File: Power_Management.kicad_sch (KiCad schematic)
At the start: 21 parts, among them J1 BATT, Q1 2N7002, SW1 POWER, U1 BQ24075RGT, U2 MAX17048

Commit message: feat(schematic): Add titles and individual sheet comments
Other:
- company: (none) -> Kurtis Lew
- title: (none) -> Conejo nRF52840 Keyboard - Power Management
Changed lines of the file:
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@@
 (kicad_sch (version 20211123) (generator eeschema)
   (paper "USLetter")
+  (title_block
+    (title "Conejo nRF52840 Keyboard - Power Management")
+    (company "Kurtis Lew")
+  )
   (junction (at 31.75 79.375) (diameter 0) (color 0 0 0 0)
   )

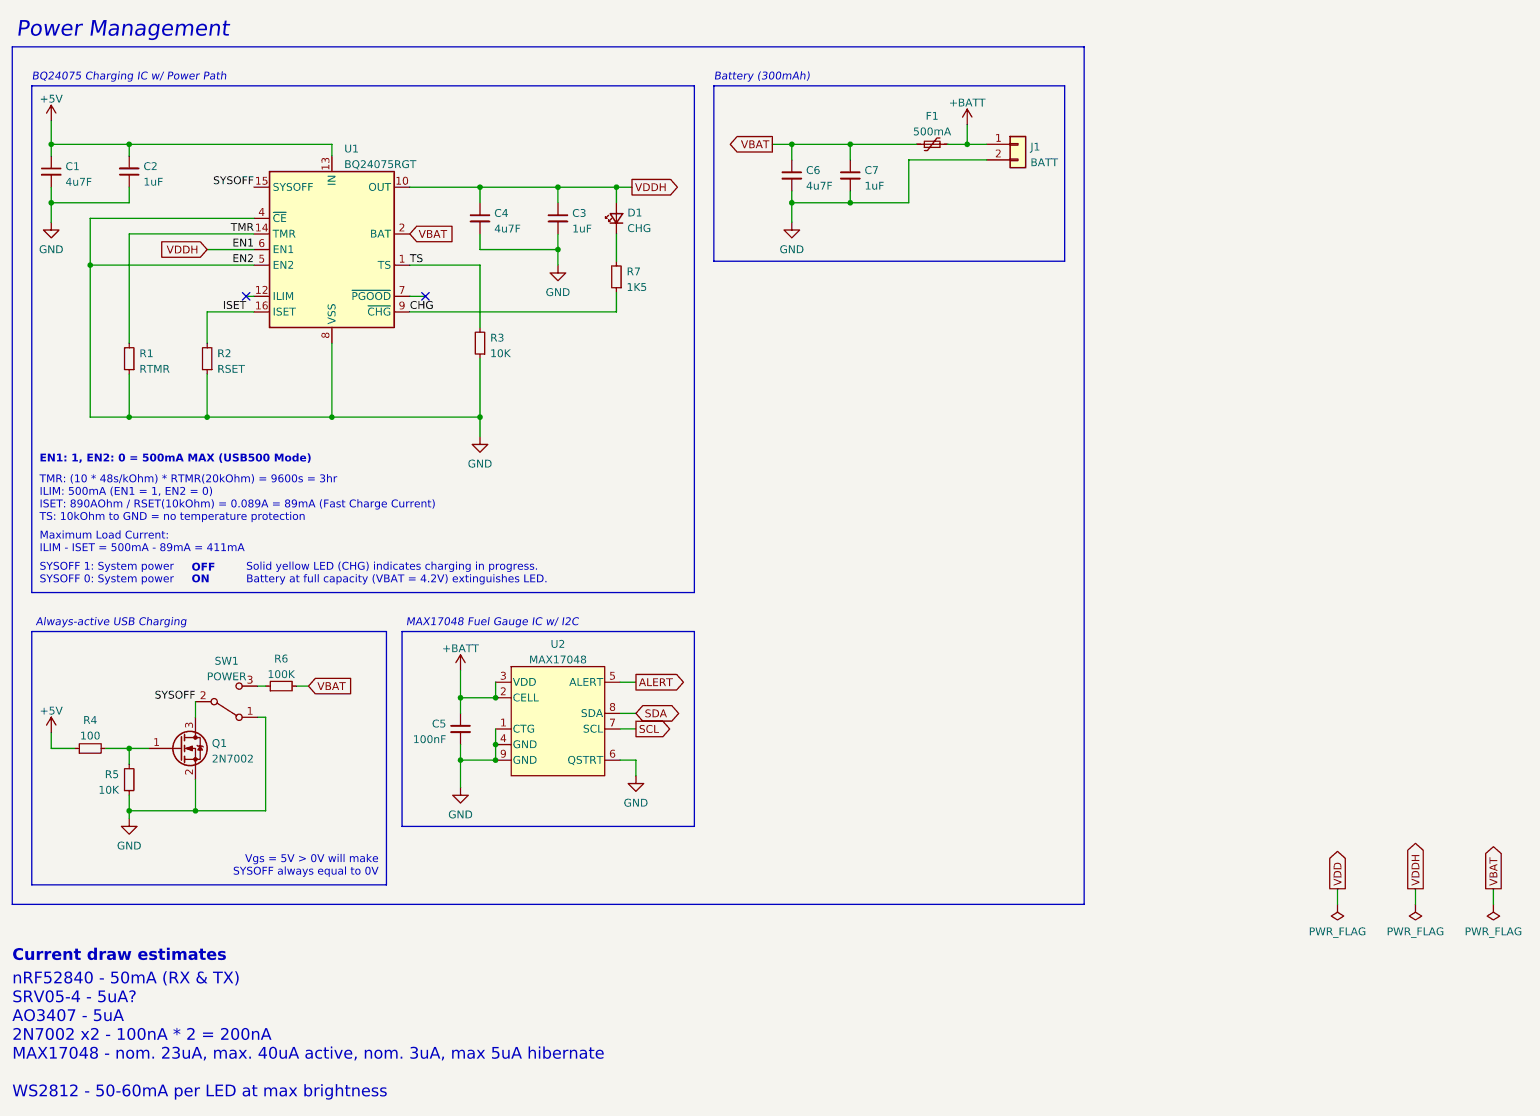
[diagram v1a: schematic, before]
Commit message: feat(pcb): Version 0.4
- Prepare to move from JLC7628 stackup to JLC3313 stackup (Lowers dielectric constant from 4.6 to 4.05)
- Increase mounting hole diameter back to 5.4mm
- 6mil signals, 10mil power, 13 mil vias
  - 3W spacing wherever possible
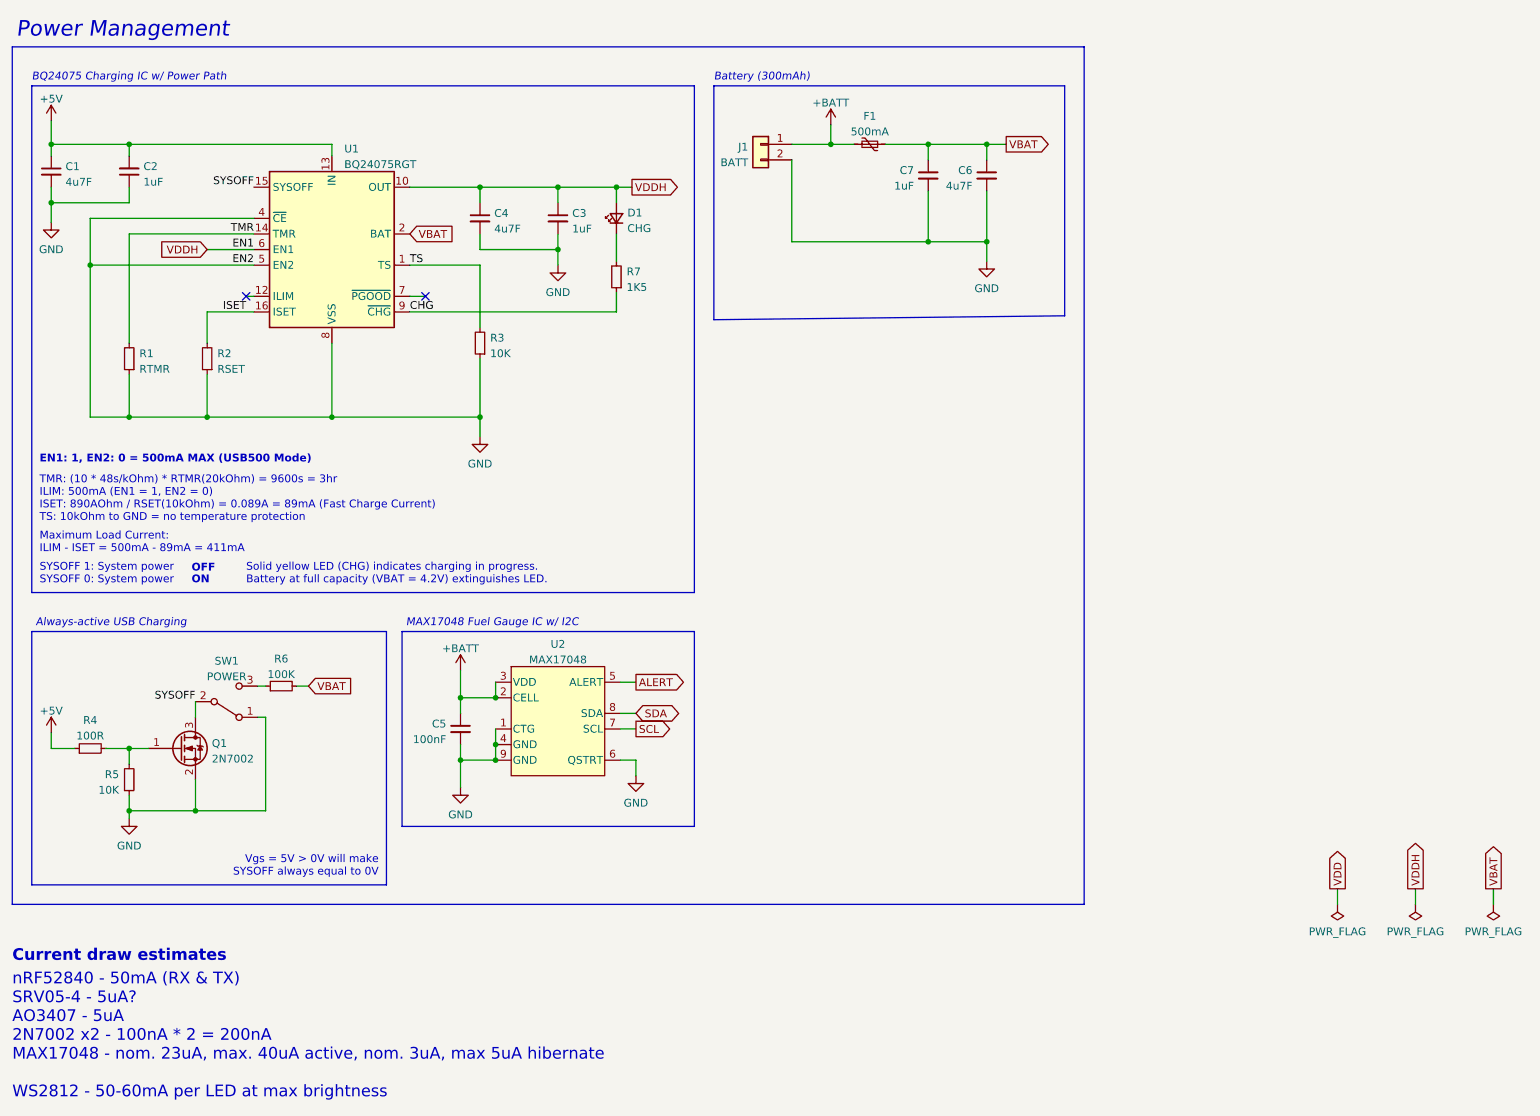
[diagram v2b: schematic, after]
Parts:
- R4: value 100 -> 100R
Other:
- moved on the sheet: C6, C7, F1, J1

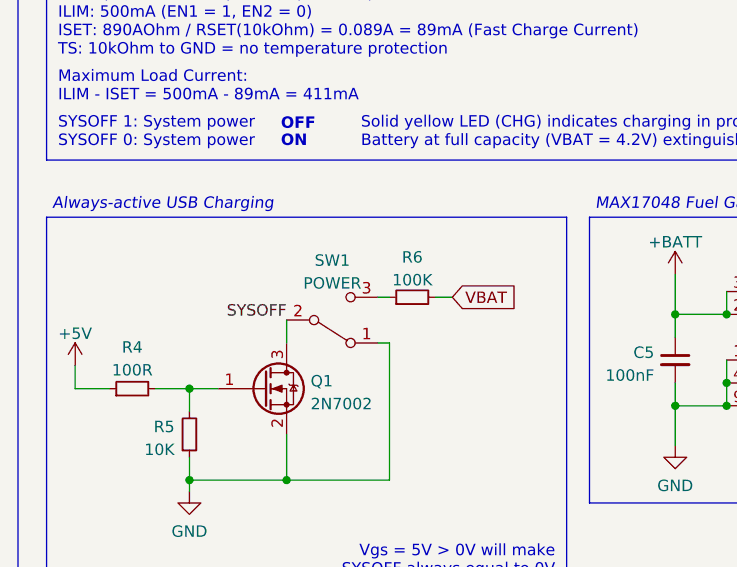
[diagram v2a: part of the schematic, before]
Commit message: feat(pcb): Version 0.4.1
- Add oscilloscope probing pads/labels
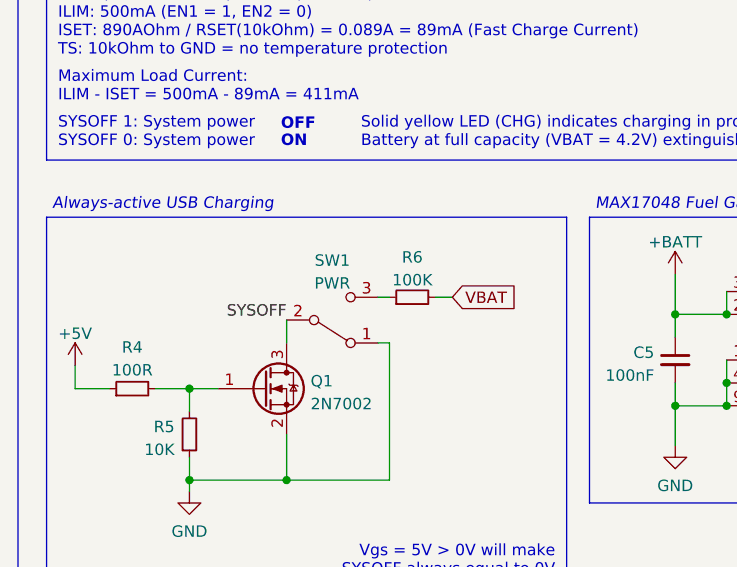
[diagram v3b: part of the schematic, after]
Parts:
- SW1: value POWER -> PWR
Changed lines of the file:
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@@
     (in_bom yes) (on_board yes) (fields_autoplaced)
     (property "Reference" "SW1" (id 0) (at 47.625 119.1092 0))
-    (property "Value" "POWER" (id 1) (at 47.625 121.6461 0))
+    (property "Value" "PWR" (id 1) (at 47.625 121.6461 0))
     (property "Footprint" "Conejo:SW_MSK12C02-HB (Reversible)" (id 2) (at 47.625 125.73 0)
       (effects (font (size 1.27 1.27)) hide)

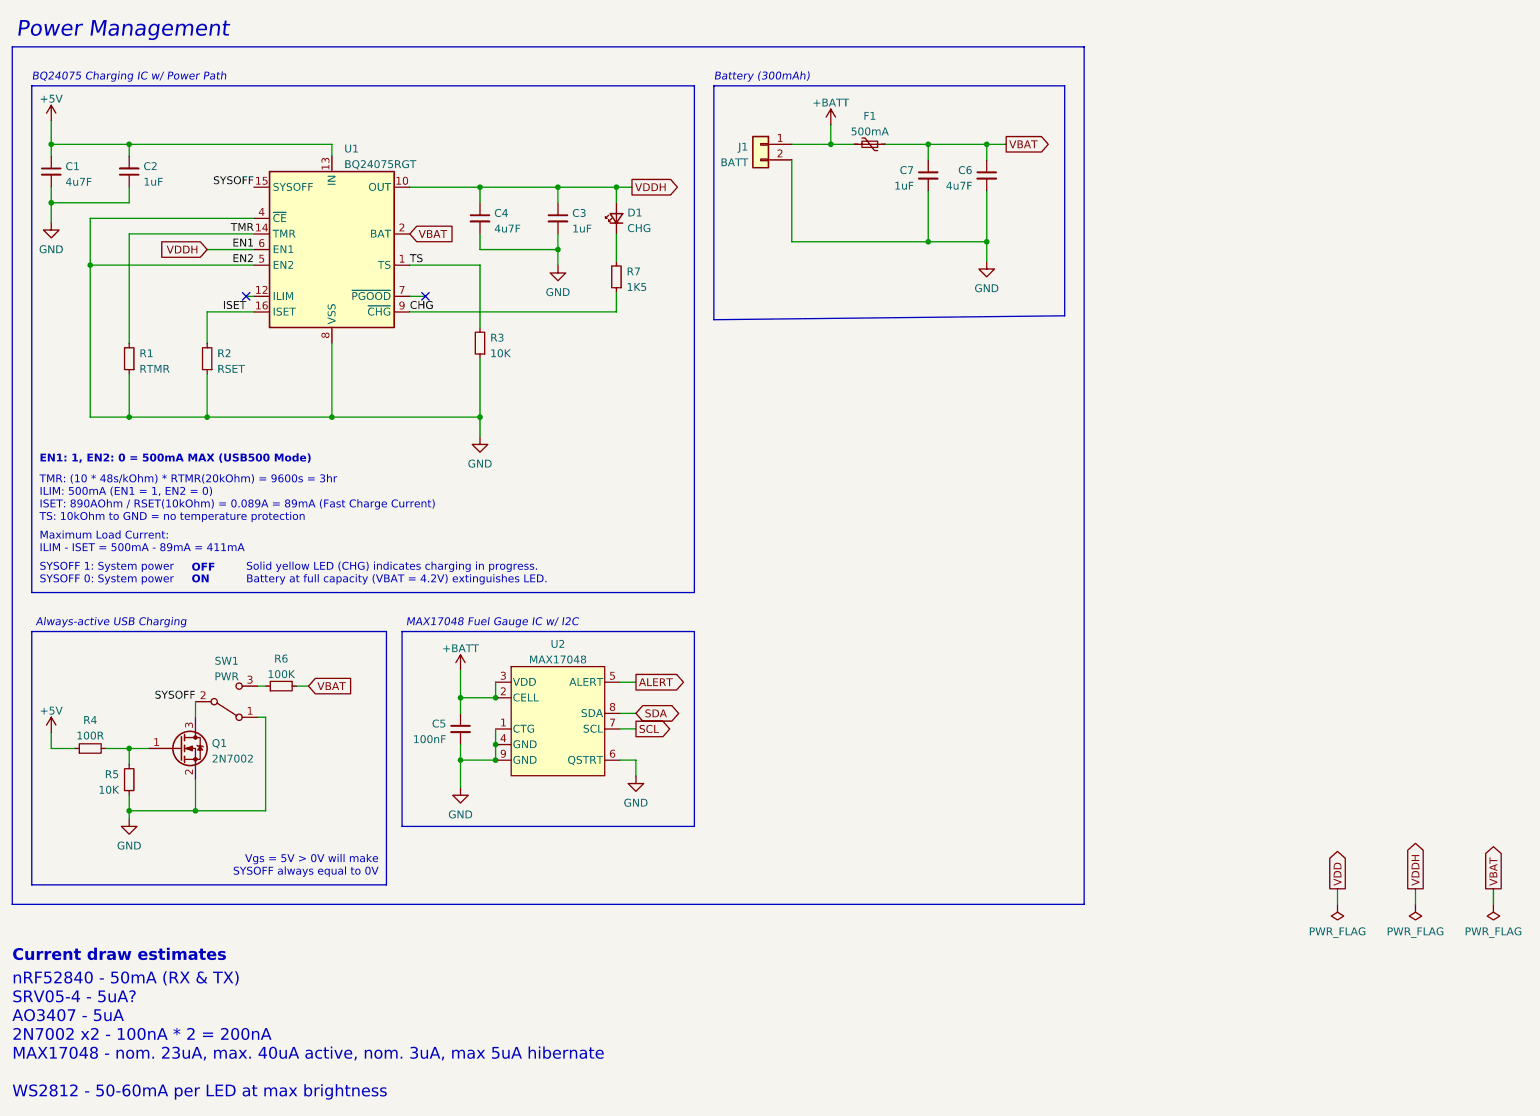
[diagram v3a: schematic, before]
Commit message: feat(pcb): Switch from 4.3mm NPTH mounting holes to M2 PTH
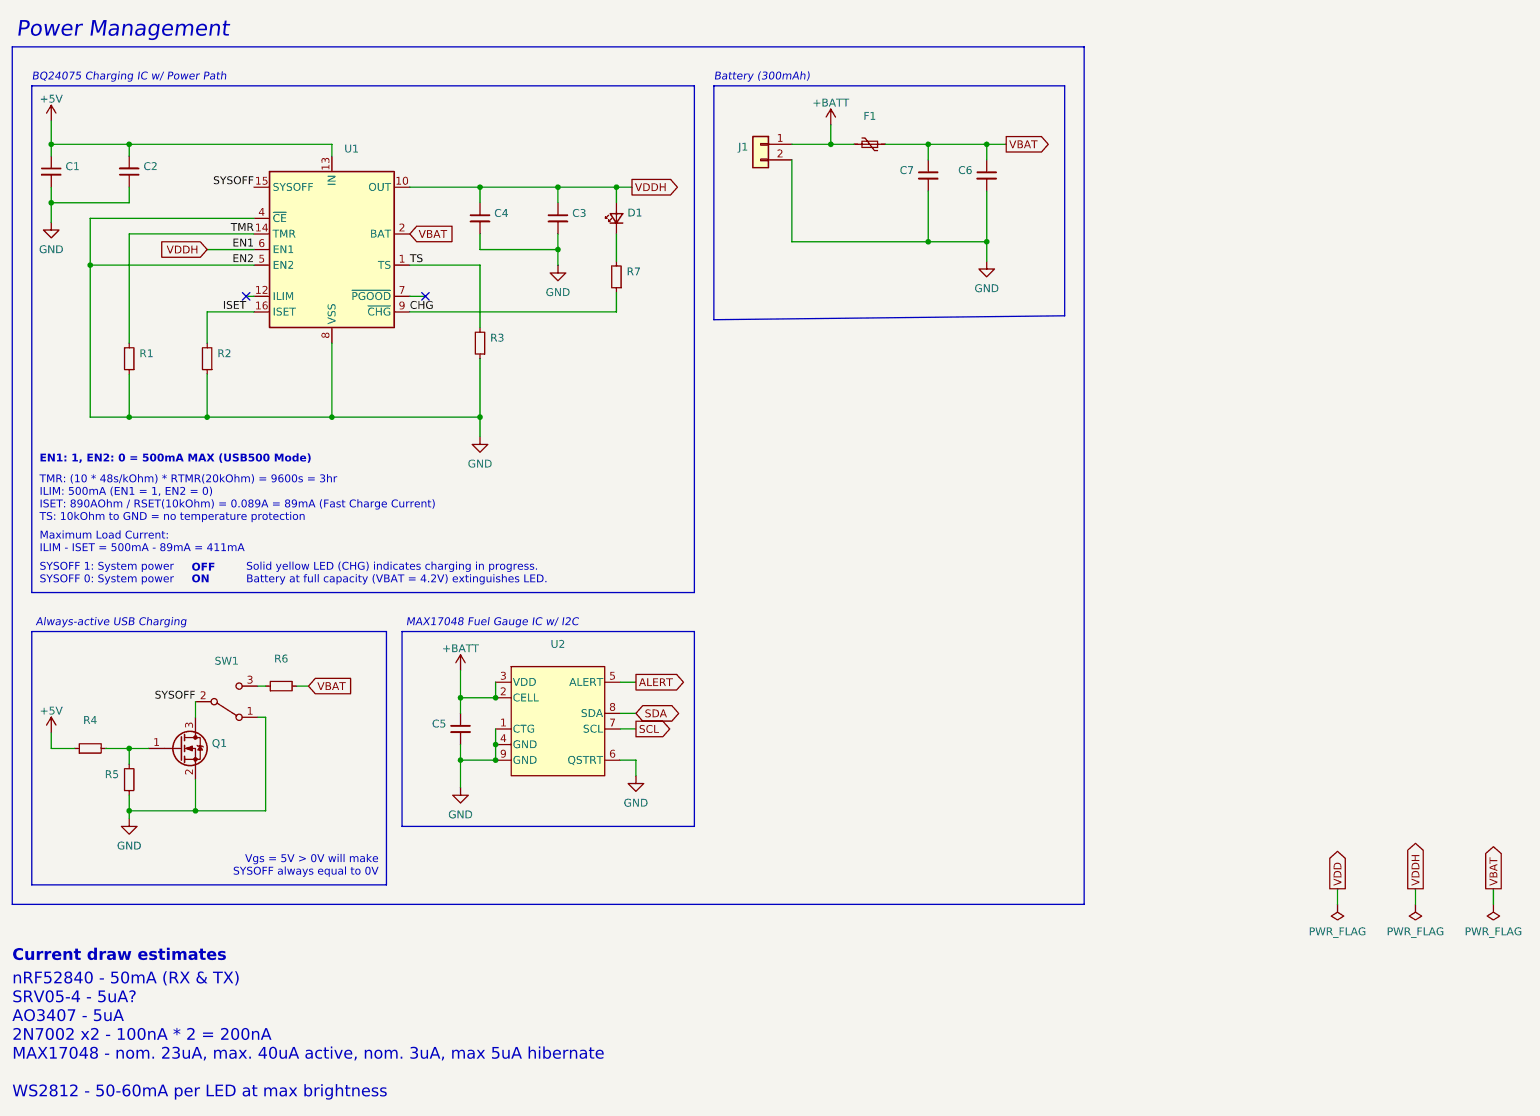
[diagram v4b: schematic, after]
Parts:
- C1, C4, C6: value 4u7F -> (none); footprint Capacitor_SMD:C_0402_1005Metric -> (none)
- C2, C3, C7: value 1uF -> (none); footprint Capacitor_SMD:C_0402_1005Metric -> (none)
- C5: value 100nF -> (none); footprint Capacitor_SMD:C_0402_1005Metric -> (none)
- D1: value CHG -> (none); footprint Conejo:LED_1206_3216Metric (Reversible) -> (none)
- F1: value 500mA -> (none); footprint Fuse:Fuse_0603_1608Metric -> (none)
- J1: value BATT -> (none); footprint Conejo:Battery Header -> (none)
- Q1: value 2N7002 -> (none); footprint Package_TO_SOT_SMD:SOT-23 -> (none)
- R1: value RTMR -> (none); footprint Resistor_SMD:R_0402_1005Metric -> (none)
- R2: value RSET -> (none); footprint Resistor_SMD:R_0402_1005Metric -> (none)
- R3, R5: value 10K -> (none); footprint Resistor_SMD:R_0402_1005Metric -> (none)
- R4: value 100R -> (none); footprint Resistor_SMD:R_0402_1005Metric -> (none)
- R6: value 100K -> (none); footprint Resistor_SMD:R_0402_1005Metric -> (none)
- R7: value 1K5 -> (none); footprint Resistor_SMD:R_0402_1005Metric -> (none)
- SW1: value PWR -> (none); footprint Conejo:SW_MSK12C02-HB (Reversible) -> (none)
- U1: value BQ24075RGT -> (none); footprint Package_DFN_QFN:VQFN-16-1EP_3x3mm_P0.5mm_EP1.6x1.6mm -> (none)
- U2: value MAX17048 -> (none); footprint Package_DFN_QFN:TDFN-8-1EP_2x2mm_P0.5mm_EP0.8x1.2mm -> (none)
